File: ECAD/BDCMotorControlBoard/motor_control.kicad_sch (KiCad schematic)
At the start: 20 parts, among them J1 Motor Connector, J4 Limit switch, J5 Limit switch, U10 PGA112, U2 DRV8870DDA, U3 INA180A1

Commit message: Progressed ECAD.
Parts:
- added C40, C41: 2u2C, Capacitor_SMD:C_0402_1005Metric, symbol Device:C
- added C42, C43: 100nC, Capacitor_SMD:C_0805_2012Metric, symbol Device:C
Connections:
- net +3.3VA: now also C38.1, U10.1 (AV_{DD}), U3.5 (V+), C40.1, C41.1, C42.1, C43.1
- net +3V0: no longer C38.1, U10.1 (AV_{DD}), U3.5 (V+)
- net GND: now also C40.2, C41.2, C42.2, C43.2

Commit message: Progressed ECAD.
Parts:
- added D3, D6: 1N4148WT, Diode_SMD:D_SOD-523, symbol Diode:1N4148WT
- added R26: 27R, symbol Device:R
- C43: value 100nC -> 2u2C; footprint Capacitor_SMD:C_0805_2012Metric -> Capacitor_SMD:C_0402_1005Metric; MPN (none) -> GRM155R60J225ME01D
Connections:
- net +3V0 is gone; now on net +3.3VA: U10.3 (CH0/V_{CAL})
- net A_SENSE: now also R26.1
- net A_SENSE_LP: now also R26.2
- net LIM1: now also C4.1, R2.1, D3.1 (K)
- net LIM2: now also C5.1, R4.1, D6.1 (K)
- net at J4.1 (Pin_1), R2.2, R3.1: now also D3.2 (A)
- net PGA_SCLK: now reaches U10.7 (SCLK)
- net PGA_DIO: now reaches U10.8 (DIO)
- net ~{PGA_CS}: now reaches U10.9 (~{CS})
- net at J5.1 (Pin_1), R4.2, R5.1: now also D6.2 (A)
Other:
- note added: "-3dB Cutoff Frequency: 117,9 kHz"
- note added: "RC Low Pass filter characteristics Input square wave max input frequency = xx Hz"
- moved on the sheet: C38, C39, C4, C40, C41, C42, C5, C6, C7, C8, C9, J1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

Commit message: Progressed ECAD.
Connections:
- net +3.3VA: no longer U10.3 (CH0/V_{CAL})
- new net +3V0: U10.3 (CH0/V_{CAL})

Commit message: Progressed ECAD.
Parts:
- removed C41: 2u2C, Capacitor_SMD:C_0402_1005Metric, symbol Device:C
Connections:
- net +3.3VA: no longer U3.5 (V+)
- net +3V0: now also U3.5 (V+)
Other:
- note added: "Low pass filter -3dB Cutoff Frequency: 117,9 kHz"
- note added: "Quiescent current analog: 450 µA maximum"
- note added: "Quiescent current: 260 µA maximum"
- note removed: "-3dB Cutoff Frequency: 117,9 kHz"
- moved on the sheet: C38, C40, C42, C43, C9

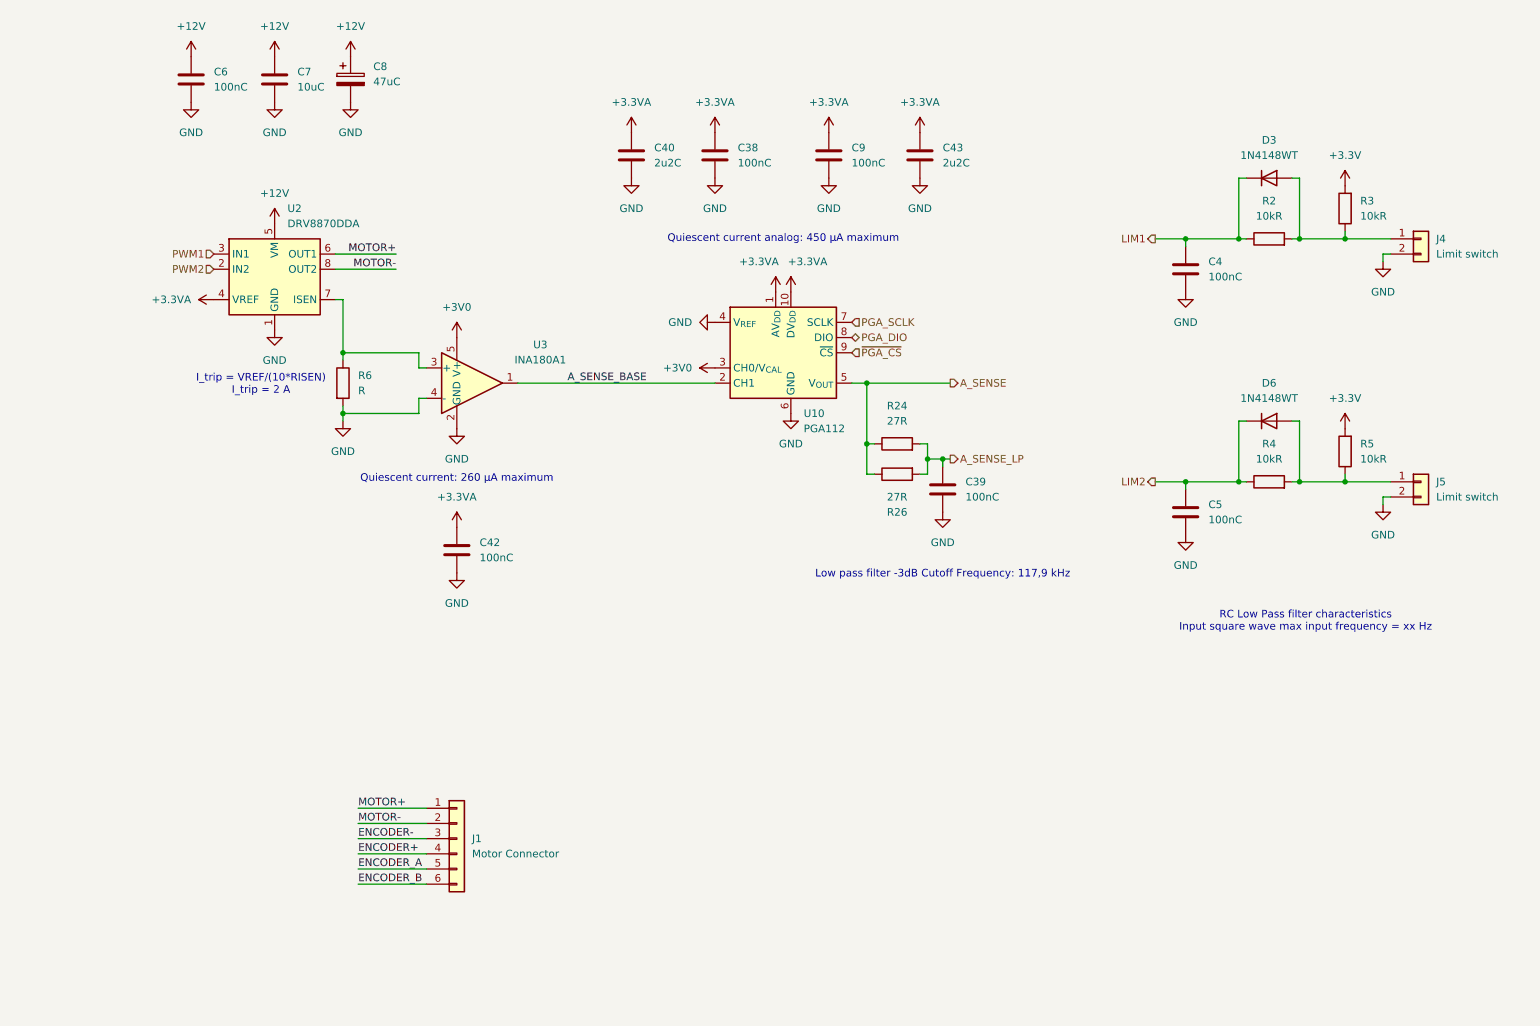
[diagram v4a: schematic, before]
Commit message: Update motor_control.kicad_sch
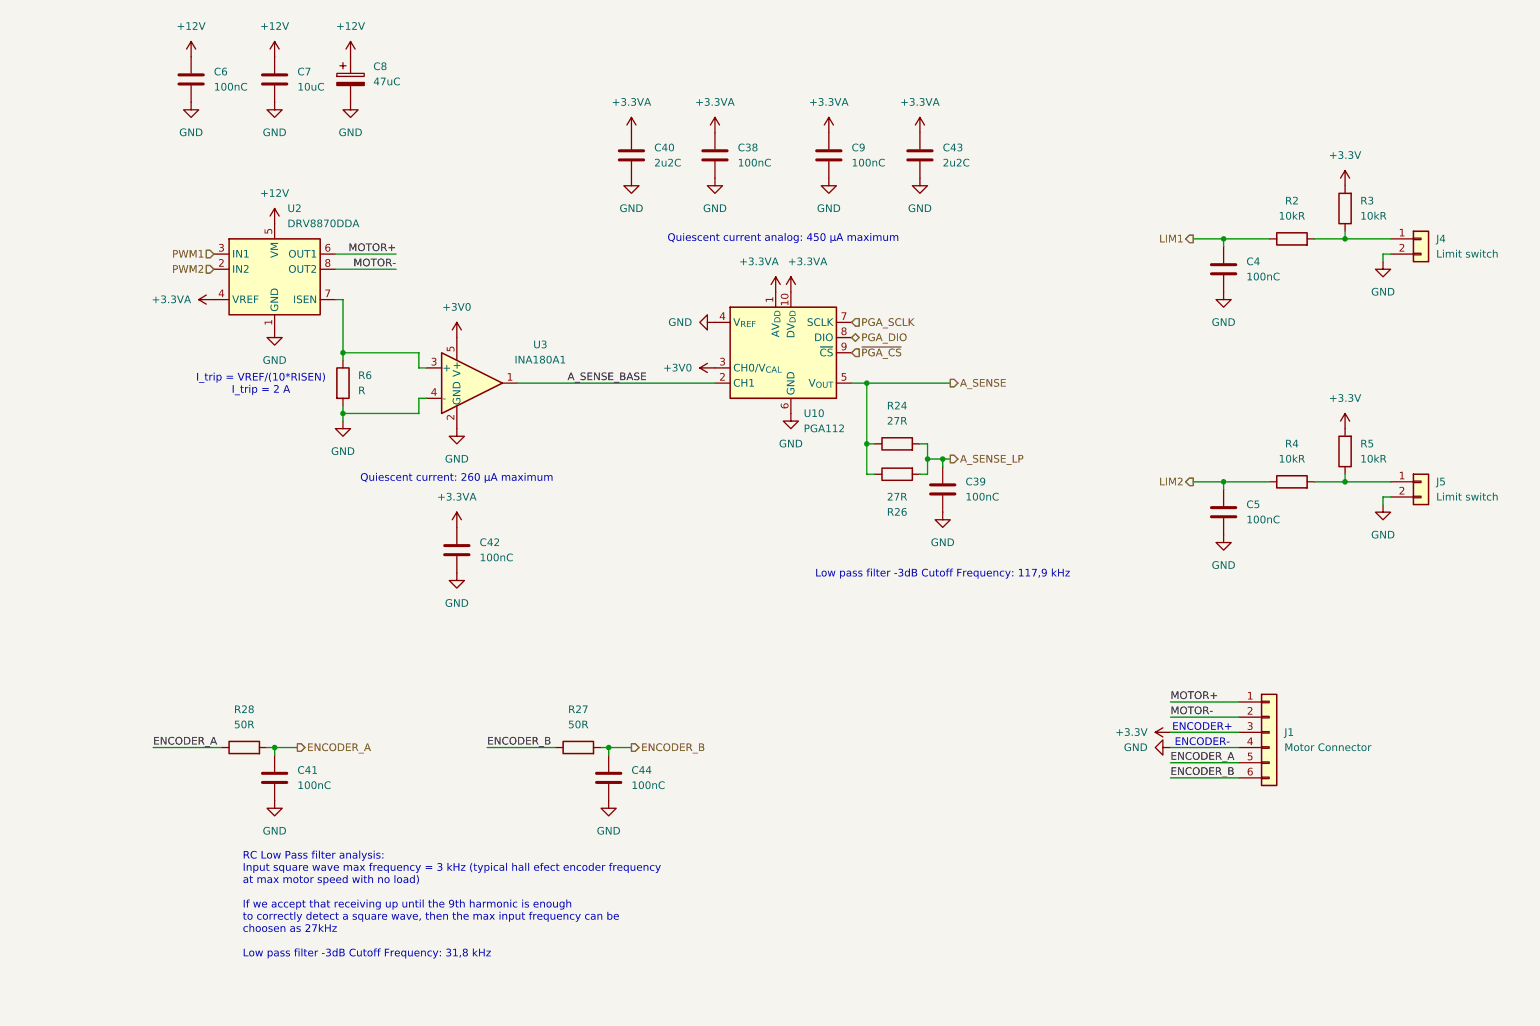
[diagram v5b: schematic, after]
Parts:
- removed D3, D6: 1N4148WT, Diode_SMD:D_SOD-523, symbol Diode:1N4148WT
- added C41, C44: 100nC, symbol Device:C
- added R27, R28: 50R, Resistor_SMD:R_0603_1608Metric, symbol Device:R
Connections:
- net ENCODER+ is gone; now on net GND: J1.4 (Pin_4)
- net ENCODER- is gone; now on net +3.3V: J1.3 (Pin_3)
- net ENCODER_A: now also C41.1, R28.1, R28.2
- net ENCODER_B: now also C44.1, R27.1, R27.2
- net GND: now also C41.2, C44.2
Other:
- note added: "ENCODER+"
- note added: "ENCODER-"
- note added: "RC Low Pass filter analysis: Input square wave max frequency = 3 kHz (typical hall efect encoder frequency at max motor speed with no load) If we accept that receiving up until the 9th harmonic is enough to correctly detect a square wave, then the max input frequency can be choosen as 27kHz Low pass filter -3dB Cutoff Frequency: 31,8 kHz"
- note removed: "RC Low Pass filter characteristics Input square wave max input frequency = xx Hz"
- moved on the sheet: C4, C5, J1, R2, R4

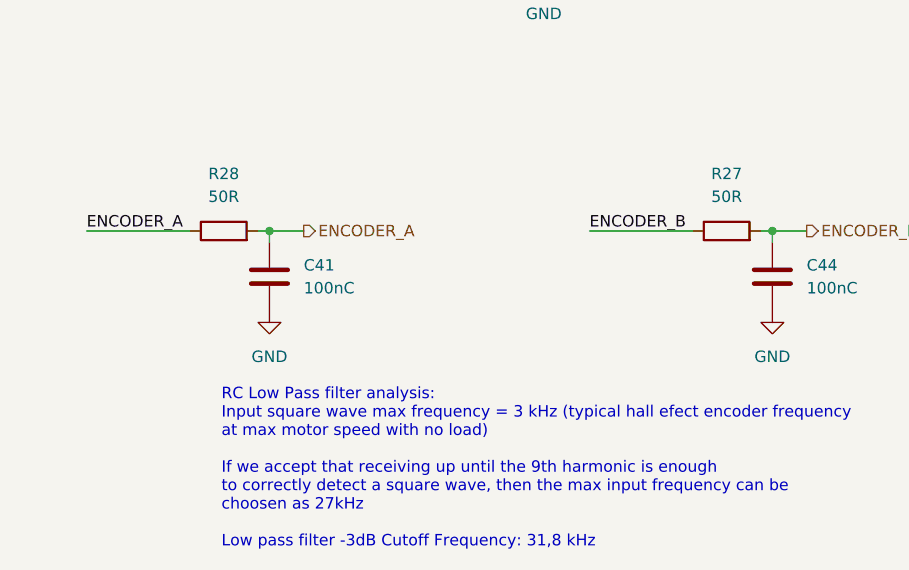
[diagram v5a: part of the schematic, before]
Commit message: Update motor_control.kicad_sch
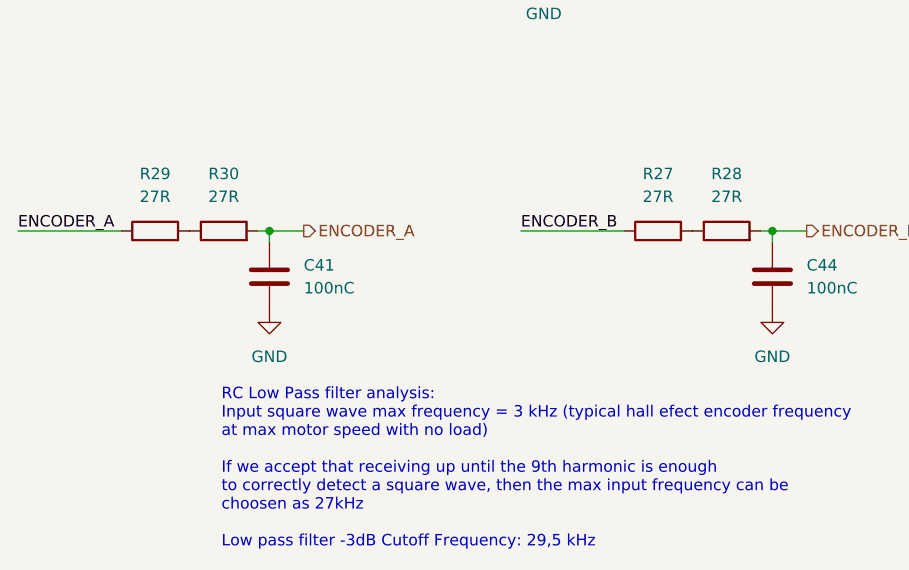
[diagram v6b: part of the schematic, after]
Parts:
- added R29, R30: 27R, Resistor_SMD:R_0201_0603Metric, symbol Device:R
- R24, R26: footprint (none) -> Resistor_SMD:R_0201_0603Metric; MPN (none) -> RC0201FR-0727RL
- R27, R28: value 50R -> 27R; footprint Resistor_SMD:R_0603_1608Metric -> Resistor_SMD:R_0201_0603Metric; MPN (none) -> RC0201FR-0727RL
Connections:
- net ENCODER_A: now also R29.1, R30.2; no longer R28.1, R28.2
- net ENCODER_B: now also R28.2; no longer R27.2
- new net: R29.2, R30.1
- new net: R27.2, R28.1
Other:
- note added: "RC Low Pass filter analysis: Input square wave max frequency = 3 kHz (typical hall efect encoder frequency at max motor speed with no load) If we accept that receiving up until the 9th harmonic is enough to correctly detect a square wave, then the max input frequency can be choosen as 27kHz Low pass filter -3dB Cutoff Frequency: 29,5 kHz"
- note removed: "RC Low Pass filter analysis: Input square wave max frequency = 3 kHz (typical hall efect encoder frequency at max motor speed with no load) If we accept that receiving up until the 9th harmonic is enough to correctly detect a square wave, then the max input frequency can be choosen as 27kHz Low pass filter -3dB Cutoff Frequency: 31,8 kHz"

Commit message: Progressed ECAD.
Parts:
- removed R26, R27, R29: 27R, Resistor_SMD:R_0201_0603Metric, symbol Device:R
- C39: value 100nC -> 2n3C
- C41, C44: value 100nC -> 15pC; footprint (none) -> Capacitor_SMD:C_0201_0603Metric; MPN (none) -> GRM0335C1E150JA01D
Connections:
- net +3V0 is gone; now on net +3.3VA: U10.3 (CH0/V_{CAL}), U3.5 (V+)
- net A_SENSE_LP is gone; now on net A_SENSE: C39.1, R24.2
- net A_SENSE: no longer R24.1, U10.5 (V_{OUT})
- net ENCODER_A: now also C41.2, R30.1; no longer C41.1
- net ENCODER_B: now also C44.2, R28.1; no longer C44.1
- net GND: now also C41.1, C44.1; no longer C41.2, C44.2
- new net: R24.1, U10.5 (V_{OUT})
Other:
- note added: "Input square wave max frequency = 3 kHz (typical hall efect encoder frequency at max motor speed with no load)"
- note added: "Low pass filter -3dB Cutoff Frequency: xx kHz"
- note removed: "Low pass filter -3dB Cutoff Frequency: 117,9 kHz"
- note removed: "RC Low Pass filter analysis: Input square wave max frequency = 3 kHz (typical hall efect encoder frequency at max motor speed with no load) If we accept that receiving up until the 9th harmonic is enough to correctly detect a square wave, then the max input frequency can be choosen as 27kHz Low pass filter -3dB Cutoff Frequency: 29,5 kHz"
- moved on the sheet: C38, C39, C4, C40, C42, C43, C5, C6, C7, C8, C9, J4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

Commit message: Progressed ECAD.
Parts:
- R24: value 27R -> 250R; MPN RC0201FR-0727RL -> (none)
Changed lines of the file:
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@@
 			)
 		)
-		(property "Value" "27R"
+		(property "Value" "250R"
 			(at 161.29 86.36 90)
 			(effects
@@
 			)
 		)
-		(property "MPN" "RC0201FR-0727RL"
+		(property "MPN" ""
 			(at 161.29 90.17 90)
 			(effects
